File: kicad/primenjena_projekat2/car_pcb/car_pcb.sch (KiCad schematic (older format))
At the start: 33 parts, among them J1 BATT_9V, J2 UART2, J3 UART1, J4 Conn_01x02, J5 Conn_01x02, J6 ICSP, SW1 SW_RST, U1 L7805, U2 DSPIC30f4013, U3 L298HN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

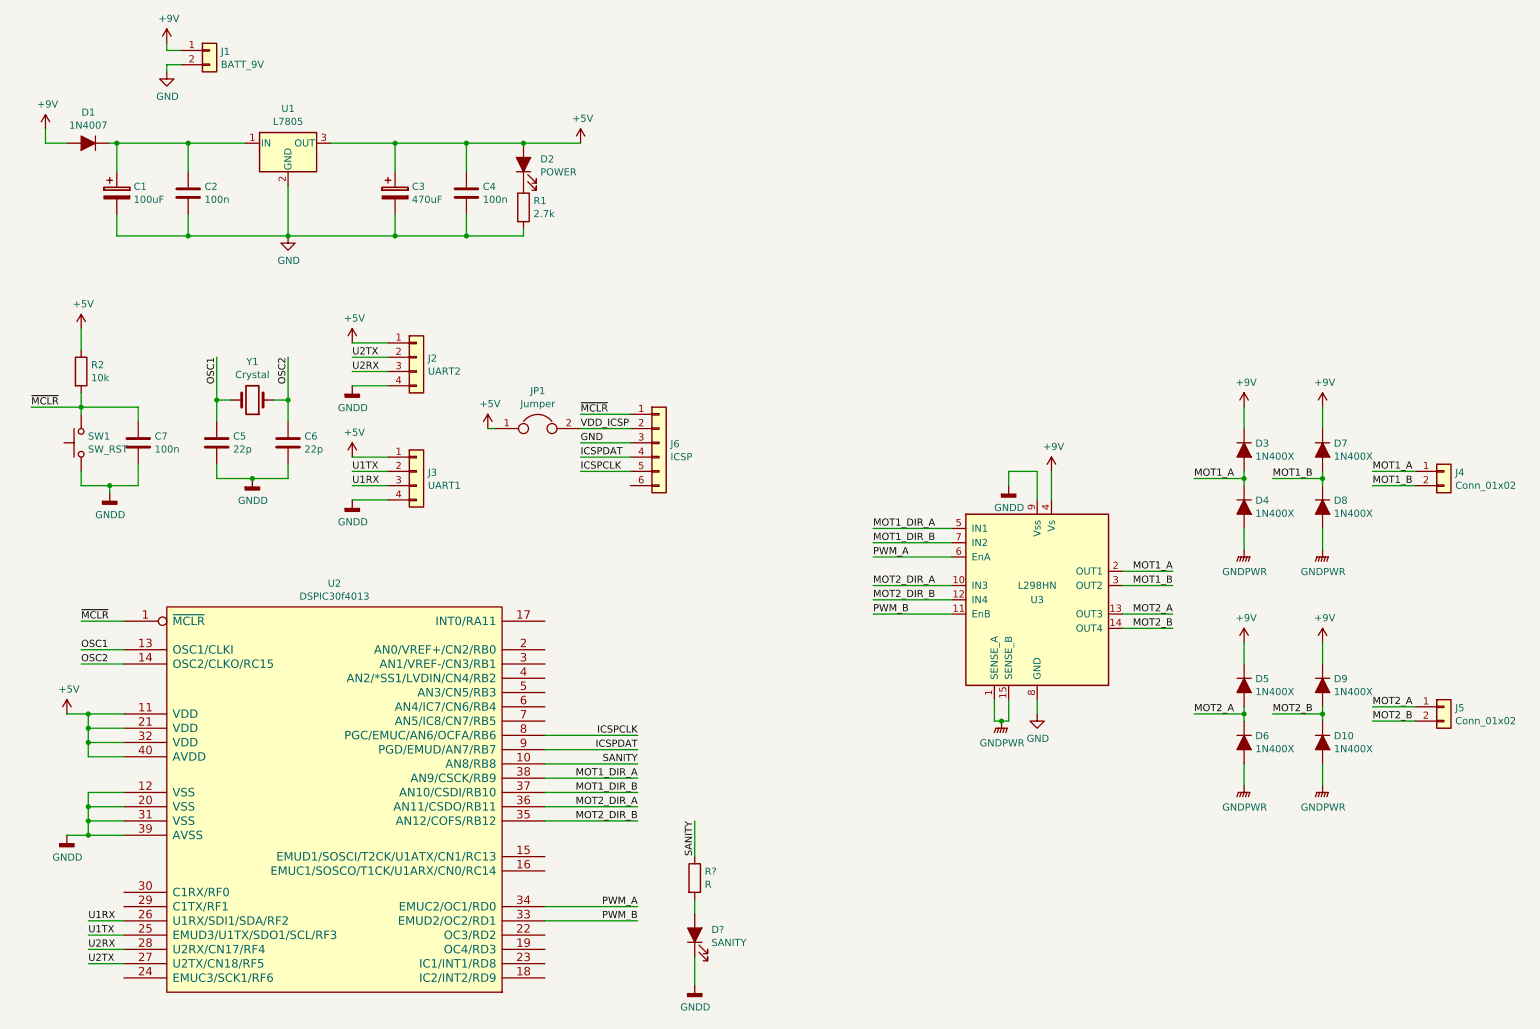
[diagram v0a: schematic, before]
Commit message: Remote control PCB
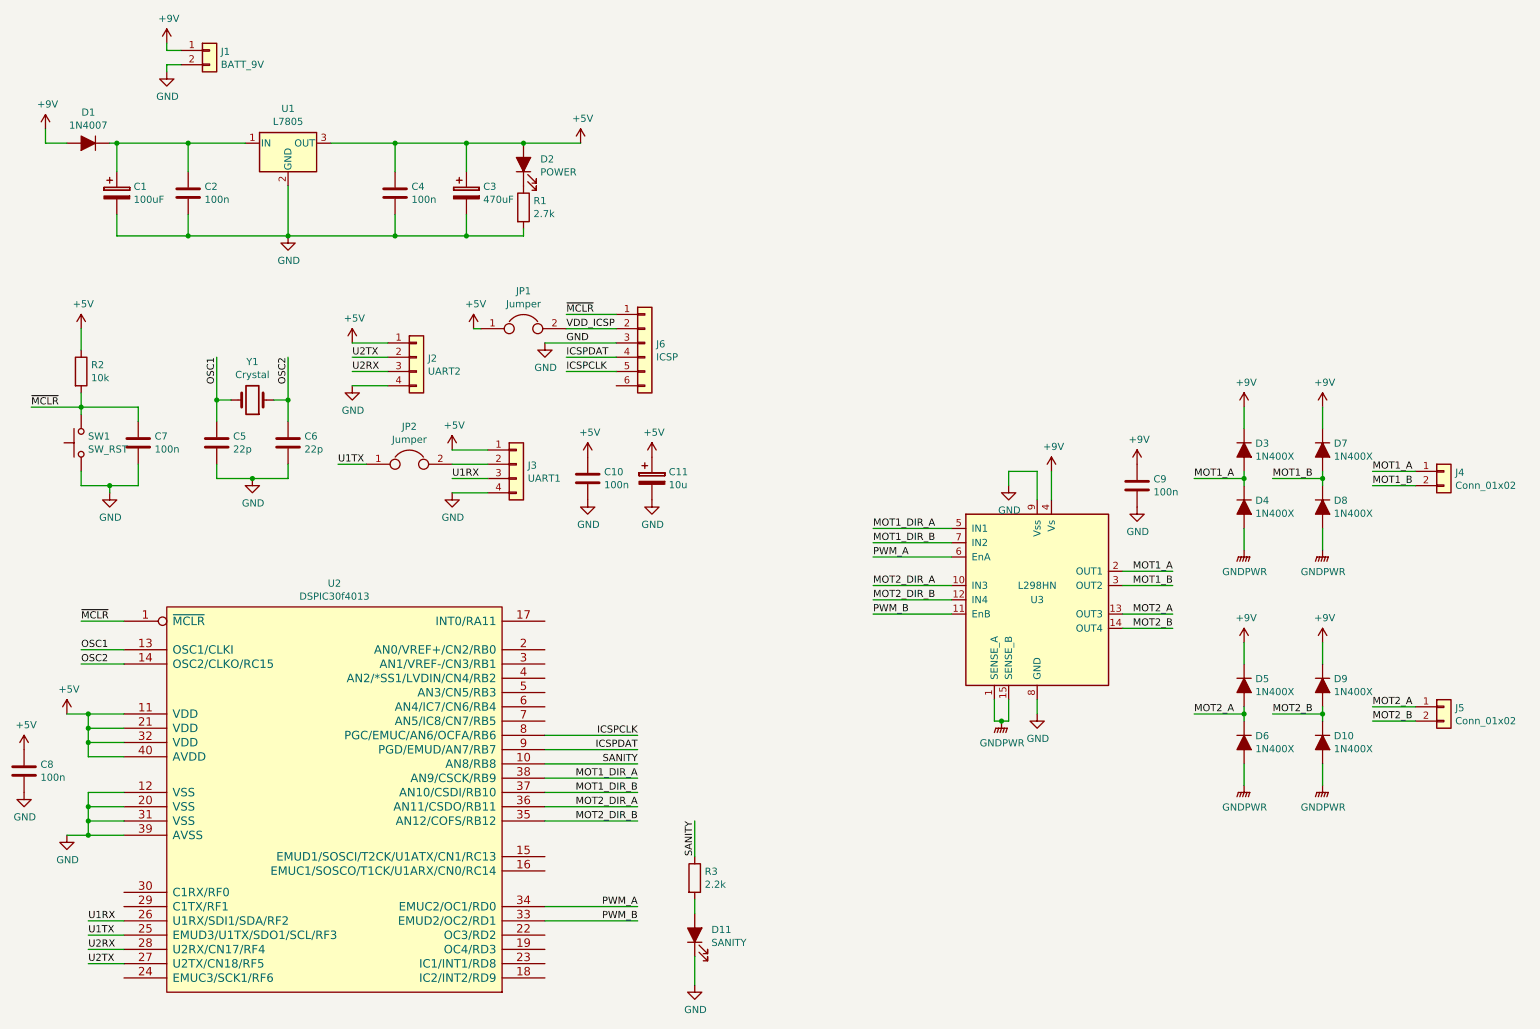
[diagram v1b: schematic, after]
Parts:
- added C10, C8, C9: 100n, symbol Device:C
- added C11: 10u, symbol Device:CP
- added JP2: Jumper, symbol Device:Jumper
- R3: renamed from R?; value R -> 2.2k
- gave numbers to parts that had none: 1
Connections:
- net GNDD is gone; now on net GND: C5.2, C6.2, C7.2, D11.1 (K), J2.4 (Pin_4), J3.4 (Pin_4), SW1.1, U2.12 (VSS), U2.20 (VSS), U2.31 (VSS), U2.39 (AVSS), U3.9 (Vss)
- net +5V: now also C10.1, C11.1, C8.1
- net +9V: now also C9.1
- net GND: now also C10.2, C11.2, C8.2, C9.2
- net U1TX: now also JP2.1; no longer J3.2 (Pin_2)
- new net: J3.2 (Pin_2), JP2.2
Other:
- moved on the sheet: C3, C4, J3, J6, JP1

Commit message: Add car PCB
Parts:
- removed C11: 10u, symbol Device:CP
- removed C9: 100n, symbol Device:C
- removed JP1: Jumper, symbol Device:Jumper
- added J7: PORTB(0-5), Connector_PinHeader_2.54mm:PinHeader_1x07_P2.54mm_Vertical, symbol Connector_Generic:Conn_01x07
- added J8: PORTB(9-11), Connector_PinHeader_2.54mm:PinHeader_1x04_P2.54mm_Vertical, symbol Connector_Generic:Conn_01x04
- added J?: PINS, Connector_PinHeader_2.54mm:PinHeader_1x04_P2.54mm_Vertical, symbol Connector_Generic:Conn_01x04
- C1, C3: footprint (none) -> Capacitor_THT:CP_Radial_D7.5mm_P2.50mm
- C10, C2, C4, C7, C8: footprint (none) -> Capacitor_THT:C_Disc_D5.0mm_W2.5mm_P5.00mm
- C5, C6: footprint (none) -> Capacitor_THT:C_Disc_D5.0mm_W2.5mm_P2.50mm
- D1: footprint (none) -> Diode_THT:D_DO-34_SOD68_P7.62mm_Horizontal
- D10, D3, D4, D5, D6, D7, D8, D9: footprint (none) -> Diode_THT:D_DO-34_SOD68_P10.16mm_Horizontal
- D11, D2: footprint (none) -> LED_THT:LED_D5.0mm
- J1: footprint (none) -> TerminalBlock:TerminalBlock_Altech_AK300-2_P5.00mm
- J2, J3: footprint (none) -> Connector_PinHeader_2.54mm:PinHeader_1x04_P2.54mm_Vertical
- J4: value Conn_01x02 -> MOT1; footprint (none) -> TerminalBlock:TerminalBlock_Altech_AK300-2_P5.00mm
- J5: value Conn_01x02 -> MOT2; footprint (none) -> TerminalBlock:TerminalBlock_Altech_AK300-2_P5.00mm
- J6: footprint (none) -> Connector_PinHeader_2.54mm:PinHeader_1x06_P2.54mm_Vertical
- JP2: footprint (none) -> Connector_PinHeader_2.54mm:PinHeader_1x02_P2.54mm_Vertical
- R1, R2, R3: footprint (none) -> Resistor_THT:R_Axial_DIN0207_L6.3mm_D2.5mm_P10.16mm_Horizontal
- SW1: footprint (none) -> Button_Switch_THT:SW_PUSH_6mm
- U1: footprint (none) -> Package_TO_SOT_THT:TO-220-3_Vertical
- U3: footprint Package_TO_SOT_THT:TO-220-15_P2.54x2.54mm_StaggerOdd_Lead4.58mm_Vertical -> footprints:TO-220-15_P2.54x2.54mm_StaggerOdd_Lead4.58mm_Vertical
- Y1: footprint (none) -> Crystal:Crystal_HC50_Vertical
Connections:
- net GNDPWR is gone; now on net GND: D10.2 (A), D4.2 (A), D6.2 (A), D8.2 (A), U3.1 (SENSE_A), U3.15 (SENSE_B)
- net GND: now also J7.7 (Pin_7), J8.4 (Pin_4), J?.4 (Pin_4)
- net MOT1_DIR_A: now also U2.35 (AN12/COFS/RB12); no longer U2.38 (AN9/CSCK/RB9)
- net MOT1_DIR_B: now also U2.34 (EMUC2/OC1/RD0); no longer U2.37 (AN10/CSDI/RB10)
- net MOT2_DIR_A: now also U2.23 (IC1/INT1/RD8); no longer U2.36 (AN11/CSDO/RB11)
- net MOT2_DIR_B: now also U2.24 (EMUC3/SCK1/RF6); no longer U2.35 (AN12/COFS/RB12)
- net PWM_A: now also U2.22 (OC3/RD2); no longer U2.34 (EMUC2/OC1/RD0)
- net SANITY: now also U2.18 (IC2/INT2/RD9); no longer U2.10 (AN8/RB8)
- net RC13: now reaches U2.15 (EMUD1/SOSCI/T2CK/U1ATX/CN1/RC13)
- net RC13: now also J?.1 (Pin_1)
- net RC14: now reaches U2.16 (EMUC1/SOSCO/T1CK/U1ARX/CN0/RC14)
- net RC14: now also J?.2 (Pin_2)
- net RA11: now reaches U2.17 (INT0/RA11)
- net RA11: now also J?.3 (Pin_3)
- net RB0: now reaches U2.2 (AN0/VREF+/CN2/RB0)
- net RB0: now also J7.1 (Pin_1)
- net RB1: now reaches U2.3 (AN1/VREF-/CN3/RB1)
- net RB1: now also J7.2 (Pin_2)
- net RB2: now reaches U2.4 (AN2/*SS1/LVDIN/CN4/RB2)
- net RB2: now also J7.3 (Pin_3)
- net RB3: now reaches U2.5 (AN3/CN5/RB3)
- net RB3: now also J7.4 (Pin_4)
- net RB4: now reaches U2.6 (AN4/IC7/CN6/RB4)
- net RB4: now also J7.5 (Pin_5)
- net RB5: now reaches U2.7 (AN5/IC8/CN7/RB5)
- net RB5: now also J7.6 (Pin_6)
- net VDD_ICSP: no longer names the net of J6.2 (Pin_2)
- new net RB10: J8.2 (Pin_2), U2.37 (AN10/CSDI/RB10)
- new net RB11: J8.1 (Pin_1), U2.36 (AN11/CSDO/RB11)
- new net RB9: J8.3 (Pin_3), U2.38 (AN9/CSCK/RB9)
